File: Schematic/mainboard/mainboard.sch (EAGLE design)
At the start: 11 parts, among them IC1 7805DT, J1 AVR_SPI_PRG_6PTH, U1 ATMEGA328P_PDIP

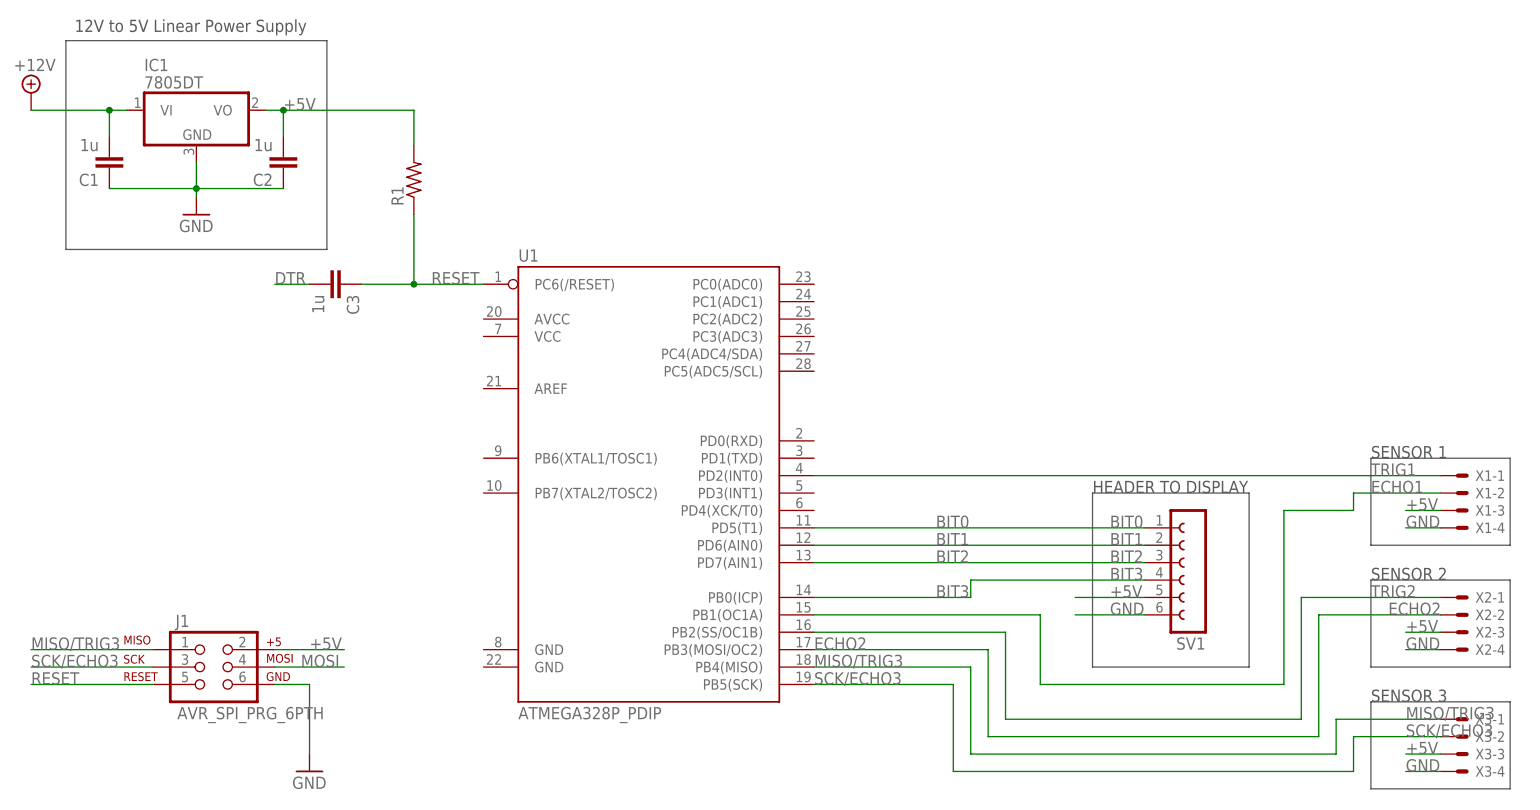
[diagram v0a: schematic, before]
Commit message: Prototype_rev4 added, schematic update. Also fixed old prototypes being overwritten, oops.
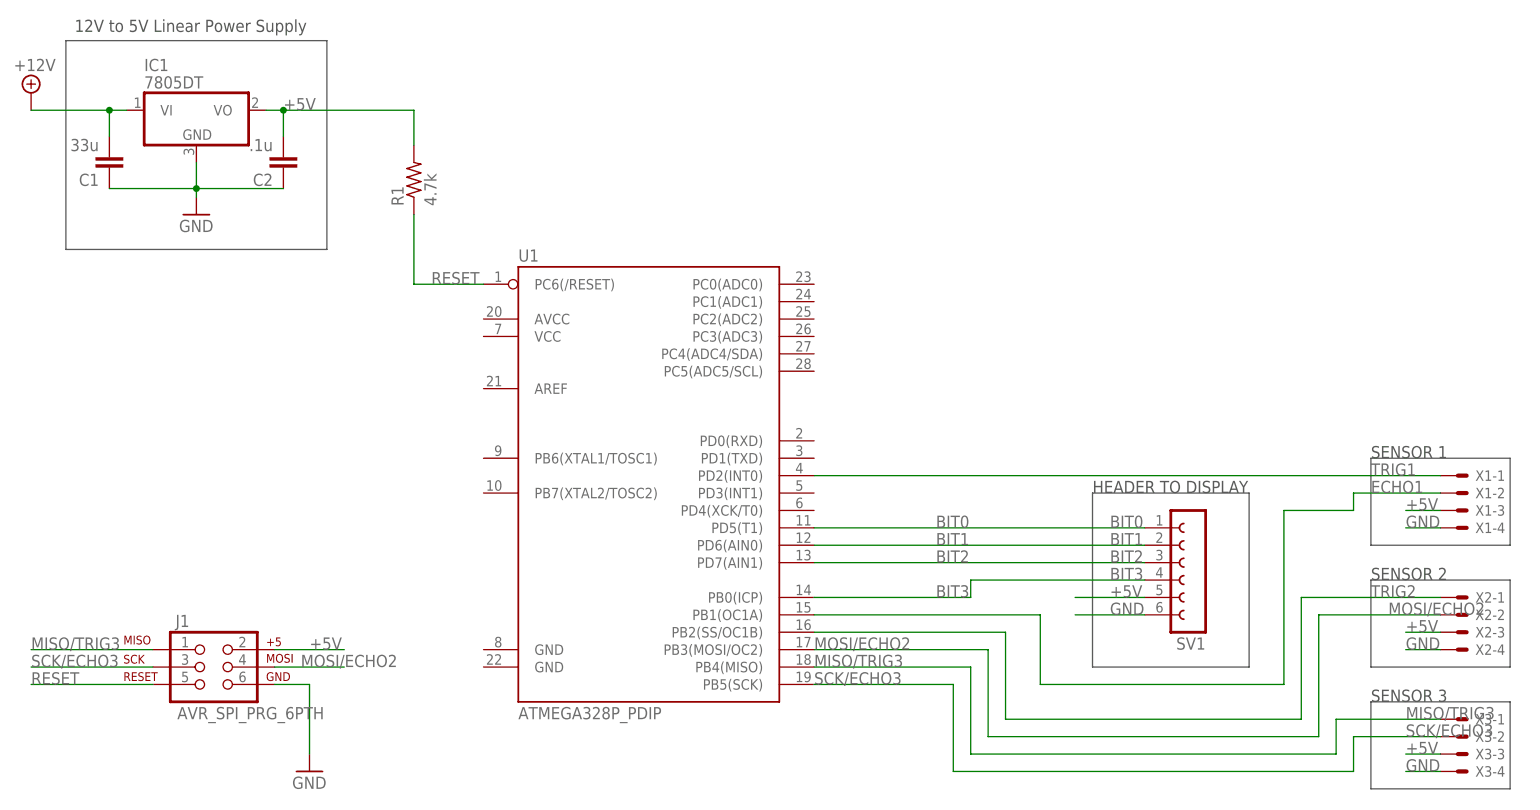
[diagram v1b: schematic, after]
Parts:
- removed C3: 1u, rcl:C-EU025-024X044
- C1: value 1u -> 33u
- C2: value 1u -> .1u
- R1: value (none) -> 4.7k
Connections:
- removed net DTR: C3.2
- removed net ECHO2: U1.PB3(MOSI/OC2), X2-2.S
- removed net MOSI: J1.4
- new net MOSI/ECHO2: J1.4, U1.PB3(MOSI/OC2), X2-2.S
- net RESET: no longer C3.1
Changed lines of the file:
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@@
 <part name="FRAME1" library="frames" deviceset="FRAME_B_L" device=""/>
 <part name="IC1" library="linear" deviceset="78*" device="DT" technology="05"/>
-<part name="C1" library="rcl" deviceset="C-EU" device="025-024X044" value="1u"/>
-<part name="C2" library="rcl" deviceset="C-EU" device="025-024X044" value="1u"/>
+<part name="C1" library="rcl" deviceset="C-EU" device="025-024X044" value="33u"/>
+<part name="C2" library="rcl" deviceset="C-EU" device="025-024X044" value=".1u"/>
 <part name="GND1" library="supply1" deviceset="GND" device=""/>
 <part name="MOTORCYCLEBATTERY" library="supply2" deviceset="+12V" device=""/>
 <part name="U1" library="SparkFun-DigitalIC" deviceset="ATMEGA328P_PDIP" device=""/>
 <part name="J1" library="SparkFun-Connectors" deviceset="AVR_SPI_PRG_6" device="PTH"/>
-<part name="R1" library="rcl" deviceset="R-US_" device="0414/5V"/>
-<part name="C3" library="rcl" deviceset="C-EU" device="025-024X044" value="1u"/>
+<part name="R1" library="rcl" deviceset="R-US_" device="0414/5V" value="4.7k"/>
 <part name="GND2" library="supply1" deviceset="GND" device=""/>
 <part name="SV1" library="con-lsta" deviceset="FE06-1" device=""/>
@@
 <instance part="J1" gate="G$1" x="35.56" y="175.26"/>
 <instance part="R1" gate="G$1" x="66.04" y="246.38" rot="R90"/>
-<instance part="C3" gate="G$1" x="55.88" y="231.14" rot="R270"/>
 <instance part="GND2" gate="1" x="50.8" y="160.02"/>
 <instance part="SV1" gate="G$1" x="180.34" y="190.5" rot="R180"/>
@@
 </segment>
 </net>
-<net name="DTR" class="0">
-<segment>
-<pinref part="C3" gate="G$1" pin="2"/>
-<wire x1="50.8" y1="231.14" x2="45.72" y2="231.14" width="0.1524" layer="91"/>
-<label x="45.72" y="231.14" size="1.778" layer="95"/>
-</segment>
-</net>
 <net name="RESET" class="0">
 <segment>
@@
 <wire x1="76.2" y1="231.14" x2="66.04" y2="231.14" width="0.1524" layer="91"/>
 <wire x1="66.04" y1="231.14" x2="66.04" y2="241.3" width="0.1524" layer="91"/>
-<wire x1="66.04" y1="231.14" x2="58.42" y2="231.14" width="0.1524" layer="91"/>
-<junction x="66.04" y="231.14"/>
-<pinref part="C3" gate="G$1" pin="1"/>
 <label x="68.58" y="231.14" size="1.778" layer="95"/>
-</segment>
-</net>
-<net name="MOSI" class="0">
-<segment>
-<pinref part="J1" gate="G$1" pin="4"/>
-<wire x1="45.72" y1="175.26" x2="55.88" y2="175.26" width="0.1524" layer="91"/>
-<label x="49.53" y="175.26" size="1.778" layer="95"/>
 </segment>
 </net>
@@
 </segment>
 </net>
-<net name="ECHO2" class="0">
+<net name="MOSI/ECHO2" class="0">
 <segment>
 <pinref part="U1" gate="G$1" pin="PB3(MOSI/OC2)"/>
@@
 <label x="208.28" y="182.88" size="1.778" layer="95"/>
 </segment>
+<segment>
+<pinref part="J1" gate="G$1" pin="4"/>
+<wire x1="45.72" y1="175.26" x2="55.88" y2="175.26" width="0.1524" layer="91"/>
+<label x="49.53" y="175.26" size="1.778" layer="95"/>
+</segment>
 </net>
 </nets>
 </sheet>
 </sheets>
+<errors>
+</errors>
 </schematic>
 </drawing>
